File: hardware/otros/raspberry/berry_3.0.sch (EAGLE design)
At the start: 11 parts

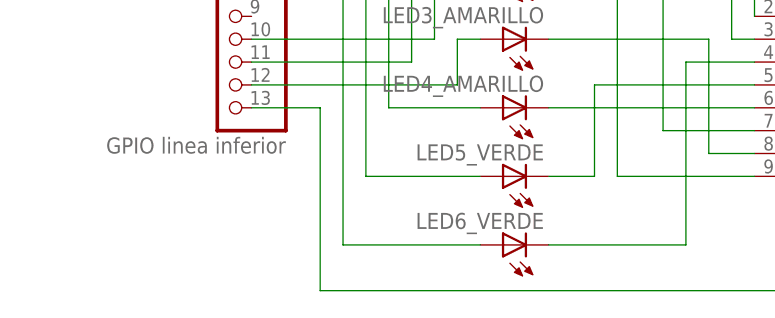
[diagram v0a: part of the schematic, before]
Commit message: 
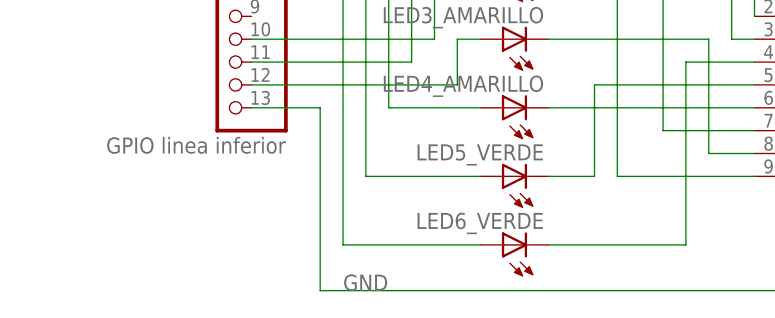
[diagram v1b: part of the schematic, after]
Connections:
- net N$5 renamed GND
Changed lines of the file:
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@@
 </segment>
 </net>
-<net name="N$5" class="0">
+<net name="GND" class="0">
 <segment>
 <pinref part="SG1" gate="G$1" pin="1"/>
@@
 <wire x1="66.04" y1="55.88" x2="73.66" y2="55.88" width="0.1524" layer="91"/>
 <junction x="73.66" y="55.88"/>
+<label x="5.08" y="25.4" size="1.778" layer="95"/>
 </segment>
 </net>
